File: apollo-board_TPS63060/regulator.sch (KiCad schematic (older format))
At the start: 45 parts, among them J11 Conn_01x04_Male, Q10 2N7002A, Q11 2N7002A, Q13 DMP2035UVT, Q14 DMP2035UVT, Q5 DMP2035UVT, Q9 2N7002A, U10 TPS63070RNMT, U9 TPS63060

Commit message: Place and route U9 (TPS63060)
+ re-place other parts
+ re-design planes shapes
+ display some silkscreen Ref. Des
+ misc. improvements.
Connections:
- net labels added: 3v3_Reg_FB, 3v3_Reg_PS, 3v3_Reg_Vaux, 3v3_Reg_Vin
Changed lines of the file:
@@
 Wire Wire Line
 	7950 1750 8150 1750
-Text Notes 5750 1650 0    50   ~ 0
+Text Notes 5750 1600 0    50   ~ 0
 PS (Power Save Mode) :\n- "0" Enabled\n- "1" Disabled
 Text Notes 7350 2750 0    50   ~ 0
@@
 R1 = R2 x (Vout / Vfb - 1)\nwith Vfb = 500mV
 Wire Notes Line
-	6850 2100 6200 2100
+	6850 2050 6200 2050
 Wire Notes Line
-	6200 2100 6200 1650
+	6200 2050 6200 1650
 Wire Notes Line
 	7600 2300 7600 2500
@@
 Wire Notes Line
 	8250 1550 8250 850
+Text Label 4950 1700 0    50   ~ 0
+3v3_Reg_Vin
+Text Label 6350 1950 0    50   ~ 0
+3v3_Reg_Vaux
+Text Label 8200 2100 0    50   ~ 0
+3v3_Reg_FB
+Text Label 6850 2150 2    50   ~ 0
+3v3_Reg_PS
 $EndSCHEMATC

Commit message: Add TPS63060 component files
+ 3D package
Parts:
- removed U9: TPS63060, Package_SON:Texas_S-PWSON-N10_ThermalVias, symbol Regulator_Switching:TPS63060
- added U9: TPS63060, TPS63060:Texas_S-PWSON-N10_ThermalVias, symbol tps63060:TPS63060
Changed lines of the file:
@@
 Wire Wire Line
 	1850 6800 2450 6800
-$Comp
-L Regulator_Switching:TPS63060 U9
-U 1 1 6035D0EB
-P 7250 1950
-F 0 "U9" H 7250 2617 50  0000 C CNN
-F 1 "TPS63060" H 7250 2526 50  0000 C CNN
-F 2 "Package_SON:Texas_S-PWSON-N10_ThermalVias" H 7250 1300 50  0001 C CNN
-F 3 "http://www.ti.com/lit/ds/symlink/tps63060.pdf" H 7250 1950 50  0001 C CNN
-	1    7250 1950
-	1    0    0    -1
-$EndComp
 Wire Wire Line
 	6850 1550 6750 1550
@@
 Text Label 6850 2150 2    50   ~ 0
 3v3_Reg_PS
+$Comp
+L tps63060:TPS63060 U9
+U 1 1 60371E4B
+P 7250 1950
+F 0 "U9" H 7250 2617 50  0000 C CNN
+F 1 "TPS63060" H 7250 2526 50  0000 C CNN
+F 2 "TPS63060:Texas_S-PWSON-N10_ThermalVias" H 7250 1300 50  0001 C CNN
+F 3 "http://www.ti.com/lit/ds/symlink/tps63060.pdf" H 7250 1950 50  0001 C CNN
+	1    7250 1950
+	1    0    0    -1
+$EndComp
 $EndSCHEMATC

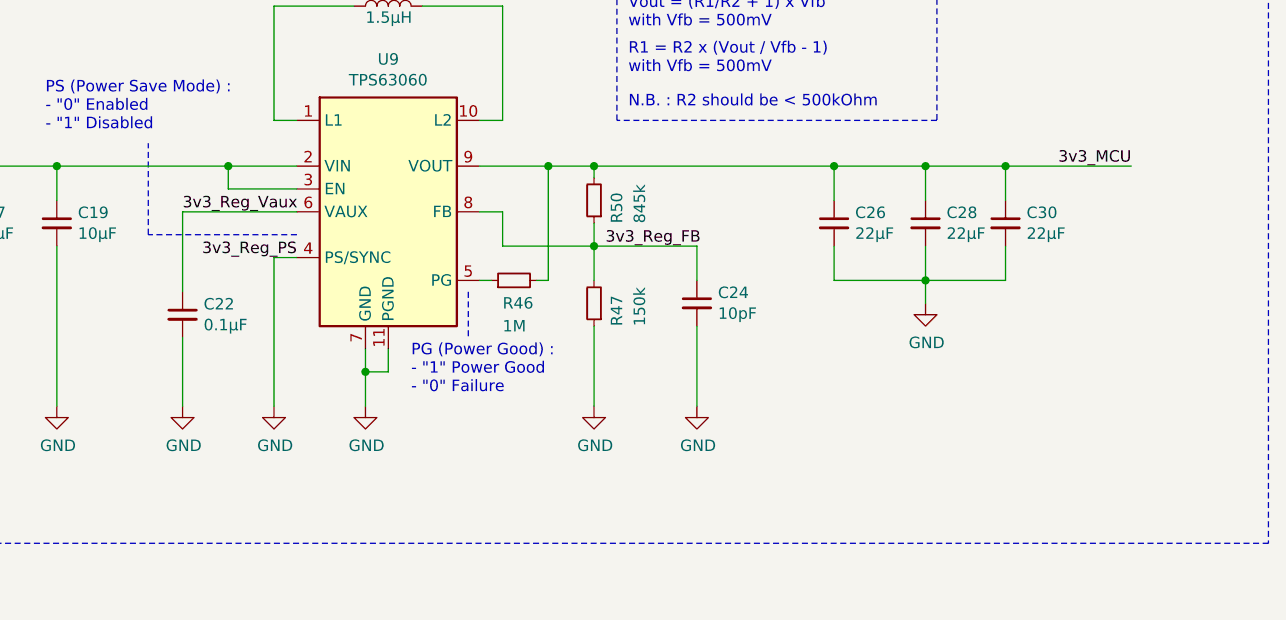
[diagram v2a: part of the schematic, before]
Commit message: Update 22µF 0805 & 100nF 0603 capacitors
around TPS63060
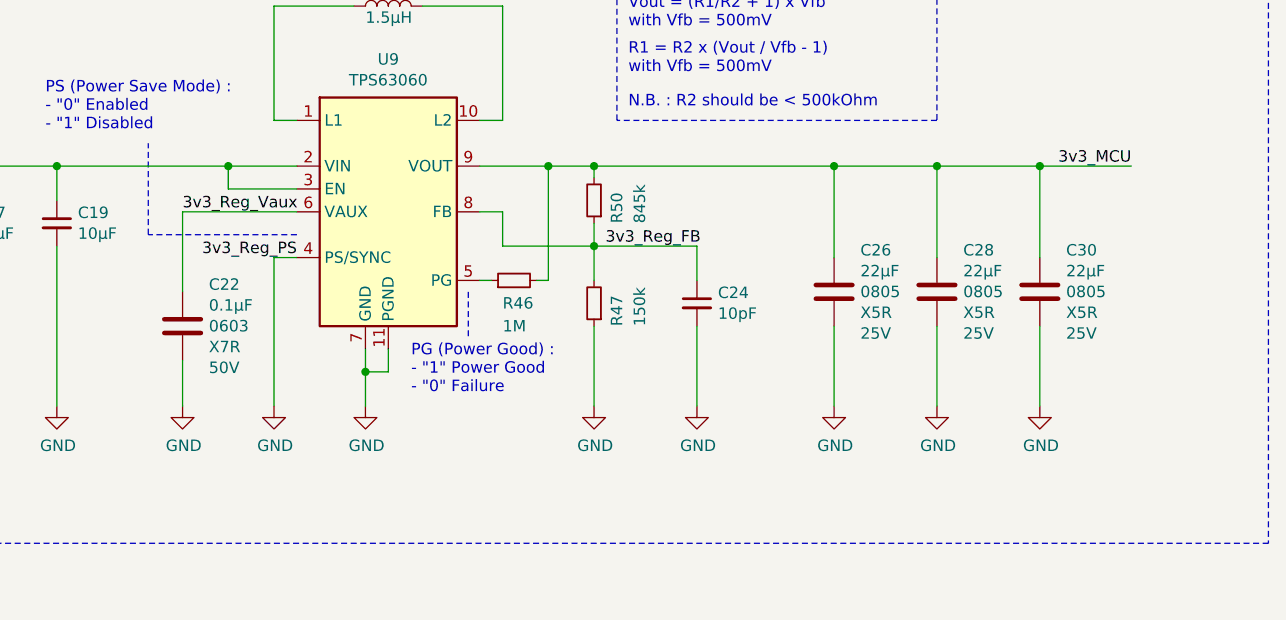
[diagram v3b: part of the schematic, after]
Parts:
- removed C22: 0.1µF, Capacitor_SMD:C_0603_1608Metric, symbol Device:C_Small
- removed C26, C28, C30: 22μF, Capacitor_SMD:C_0805_2012Metric, symbol Device:C_Small
- added C22: CL10B104KB8NNNC, Capacitor_SMD:C_0603_1608Metric, symbol cl10b104kb8nnnc:CL10B104KB8NNNC
- added C26, C28, C30: CL21A226MAQNNNE, Capacitor_SMD:C_0805_2012Metric, symbol cl21a226maqnnne:CL21A226MAQNNNE
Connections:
- net 3v3_MCU: now also C26.1, C28.1, C30.1
- net 3v3_Reg_Vaux: now also C22.1
- net GND: now also C22.2, C26.2, C28.2, C30.2

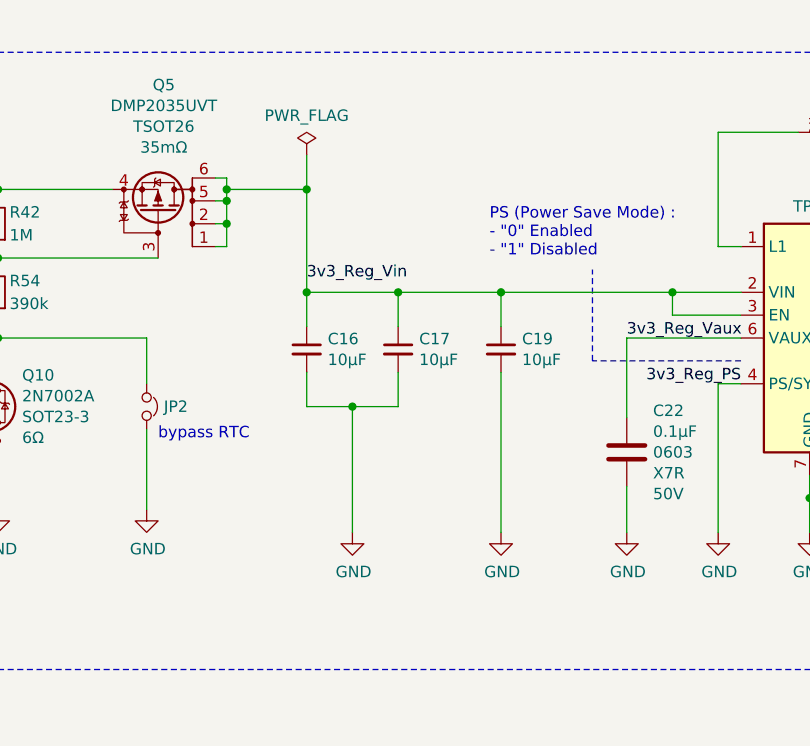
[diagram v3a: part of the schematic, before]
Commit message: Update 10µF 0805 capacitors
Around TPS63060
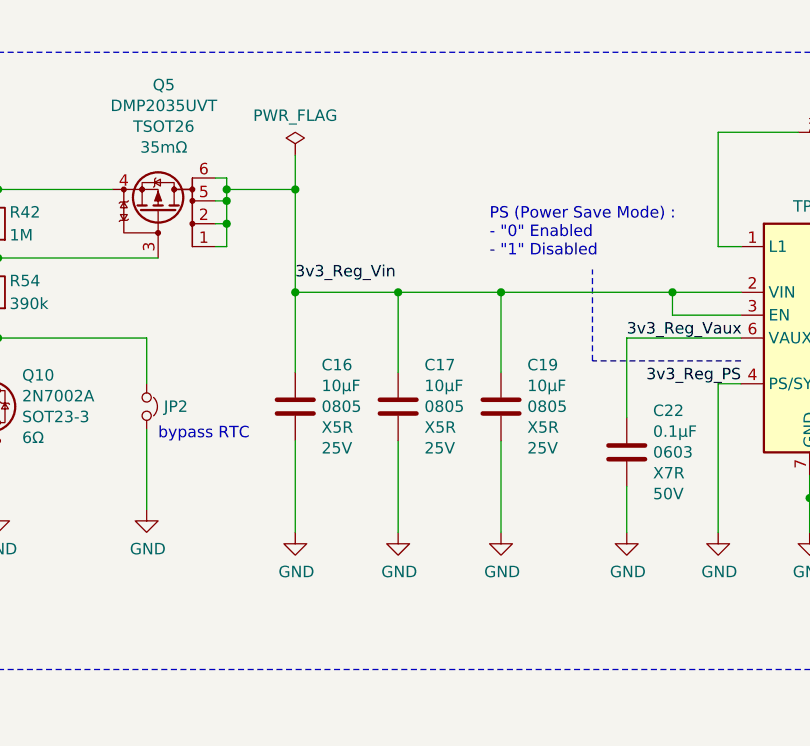
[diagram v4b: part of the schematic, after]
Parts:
- removed C16, C17, C19: 10μF, Capacitor_SMD:C_0805_2012Metric, symbol Device:C_Small
- added C16, C17, C19: CL21A106KAYNNNE, Capacitor_SMD:C_0805_2012Metric, symbol cl21a106kaynnne:CL21A106KAYNNNE
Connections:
- net 3v3_Reg_Vin: now also C16.1, C17.1, C19.1
- net GND: now also C16.2, C17.2, C19.2

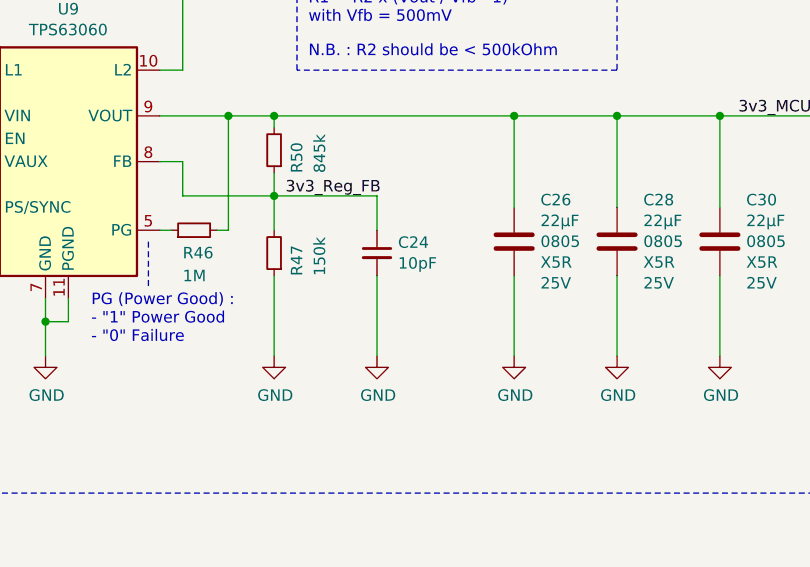
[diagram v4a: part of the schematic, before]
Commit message: Update 10pF 0603 capacitor
around TPS63060
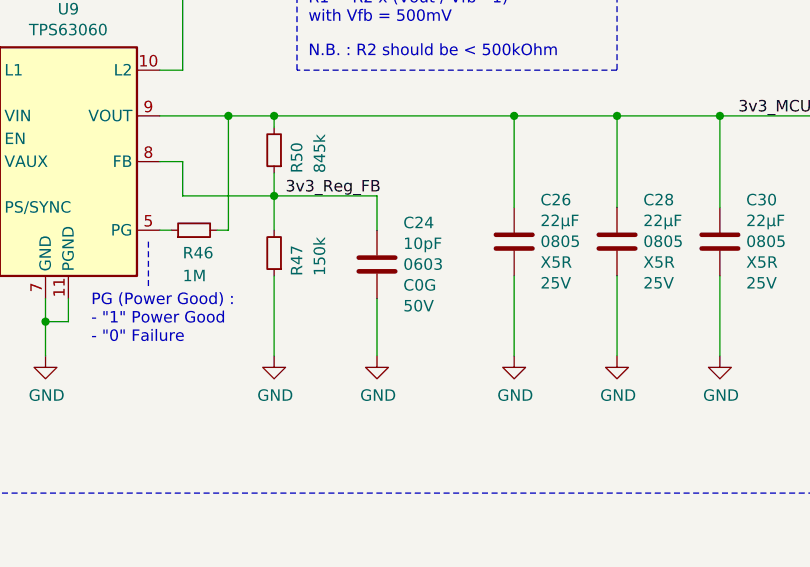
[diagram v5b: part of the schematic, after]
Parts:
- removed C24: 10pF, Capacitor_SMD:C_0603_1608Metric, symbol Device:C_Small
- added C24: CC0603JRNPO9BN100, Capacitor_SMD:C_0603_1608Metric, symbol cc0603jrnpo9bn100:CC0603JRNPO9BN100
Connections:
- net 3v3_Reg_FB: now also C24.1
- net GND: now also C24.2
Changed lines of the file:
@@
-$EndComp
-$Comp
-L Device:C_Small C24
-U 1 1 5FF33363
-P 8600 2350
-F 0 "C24" H 8692 2396 50  0000 L CNN
-F 1 "10pF" H 8692 2305 50  0000 L CNN
-F 2 "Capacitor_SMD:C_0603_1608Metric" H 8600 2350 50  0001 C CNN
-F 3 "~" H 8600 2350 50  0001 C CNN
-	1    8600 2350
-	1    0    0    -1
 $EndComp
 $Comp
@@
 $EndComp
 Wire Wire Line
-	8600 2450 8600 2800
+	8600 2550 8600 2800
 $Comp
 L power:GND #PWR079
@@
 Wire Wire Line
 	4900 2800 4900 2400
+$Comp
+L cc0603jrnpo9bn100:CC0603JRNPO9BN100 C24
+U 1 1 604E718C
+P 8600 2400
+F 0 "C24" H 8715 2582 50  0000 L CNN
+F 1 "CC0603JRNPO9BN100" H 8625 2300 50  0001 L CNN
+F 2 "Capacitor_SMD:C_0603_1608Metric" H 8638 2250 50  0001 C CNN
+F 3 "https://www.mouser.fr/datasheet/2/447/yageo_yago_s_a0009251638_1-1991554.pdf" H 8600 2400 50  0001 C CNN
+F 4 "Yageo" H 8600 2400 50  0001 C CNN "Mfr_name"
+F 5 "CC0603JRNPO9BN100" H 8600 2400 50  0001 C CNN "Mfr_no"
+F 6 "10pF" H 8715 2491 50  0000 L CNN "cap_Value"
+F 7 "0603" H 8715 2400 50  0000 L CNN "Package"
+F 8 "C0G" H 8715 2309 50  0000 L CNN "cap_Dielectric"
+F 9 "50V" H 8715 2218 50  0000 L CNN "cap_Voltage"
+F 10 "https://octopart.com/cc0603jrnpo9bn100-yageo-39467668?r=sp#PriceAndStock" H 8600 2400 50  0001 C CNN "Octopart_link"
+F 11 "https://fr.farnell.com/yageo/cc0603jrnpo9bn100/cond-10pf-50v-5-c0g-np0-0603/dp/721967?st=CC0603JRNPO9BN100" H 8600 2400 50  0001 C CNN "Farnell_link"
+F 12 "721967" H 8600 2400 50  0001 C CNN "Farnell_ref"
+F 13 "2021-02-24" H 8600 2400 50  0001 C CNN "Farnell_check_date"
+F 14 "-" H 8600 2400 50  0001 C CNN "Farnell_price_qt=1"
+F 15 "0,0405 €" H 8600 2400 50  0001 C CNN "Farnell_price_qt=10"
+F 16 "0,0203 €" H 8600 2400 50  0001 C CNN "Farnell_price_qt=100"
+F 17 "0,0135 €" H 8600 2400 50  0001 C CNN "Farnell_price_qt=1000"
+F 18 "1,951,669" H 8600 2400 50  0001 C CNN "Farnell_stock"
+F 19 "https://lcsc.com/product-detail/Multilayer-Ceramic-Capacitors-MLCC-SMD-SMT_YAGEO-CC0603JRNPO9BN100_C106245.html" H 8600 2400 50  0001 C CNN "LCSC_link"
+F 20 "C106245" H 8600 2400 50  0001 C CNN "LCSC_ref"
+F 21 "2021-02-24" H 8600 2400 50  0001 C CNN "LCSC_check_date"
+F 22 "-" H 8600 2400 50  0001 C CNN "LCSC_price_qt=1"
+F 23 "-" H 8600 2400 50  0001 C CNN "LCSC_price_qt=10"
+F 24 "$0.0038" H 8600 2400 50  0001 C CNN "LCSC_price_qt=100"
+F 25 "$0.0029" H 8600 2400 50  0001 C CNN "LCSC_price_qt=1000"
+F 26 "1,595,200" H 8600 2400 50  0001 C CNN "LCSC_stock"
+F 27 "https://www.mouser.fr/ProductDetail/Yageo/CC0603JRNPO9BN100/?qs=%2Fha2pyFaduiZbois2HzNxfUPtExZ87ifpI77BjZxylV95W8Cxrl2Iw%3D%3D" H 8600 2400 50  0001 C CNN "Mouser_link"
+F 28 "603-C0603JRNPO9BN100" H 8600 2400 50  0001 C CNN "Mouser_ref"
+F 29 "2021-02-24" H 8600 2400 50  0001 C CNN "Mouser_check_date"
+F 30 "$0.238" H 8600 2400 50  0001 C CNN "Mouser_price_qt=1"
+F 31 "-" H 8600 2400 50  0001 C CNN "Mouser_price_qt=10"
+F 32 "-" H 8600 2400 50  0001 C CNN "Mouser_price_qt=100"
+F 33 "-" H 8600 2400 50  0001 C CNN "Mouser_price_qt=1000"
+F 34 "494,335" H 8600 2400 50  0001 C CNN "Mouser_stock"
+F 35 "https://fr.rs-online.com/web/p/condensateurs-ceramique-multicouches/2006466/" H 8600 2400 50  0001 C CNN "RS_link"
+F 36 "200-6466" H 8600 2400 50  0001 C CNN "RS_ref"
+F 37 "2021-02-24" H 8600 2400 50  0001 C CNN "RS_check_date"
+F 38 "-" H 8600 2400 50  0001 C CNN "RS_price_qt=1"
+F 39 "-" H 8600 2400 50  0001 C CNN "RS_price_qt=10"
+F 40 "-" H 8600 2400 50  0001 C CNN "RS_price_qt=100"
+F 41 "0,006 € (qt=4000)" H 8600 2400 50  0001 C CNN "RS_price_qt=1000"
+F 42 "-" H 8600 2400 50  0001 C CNN "RS_stock"
+F 43 "TO_CHECK" H 8600 2400 50  0001 C CNN "Status"
+F 44 "1.03" H 8600 2400 50  0001 C CNN "Release_version"
+F 45 "2020-12-21" H 8600 2400 50  0001 C CNN "Release_date"
+F 46 "ManWithNoName" H 8600 2400 50  0001 C CNN "Designer"
+	1    8600 2400
+	1    0    0    -1
+$EndComp
 $EndSCHEMATC

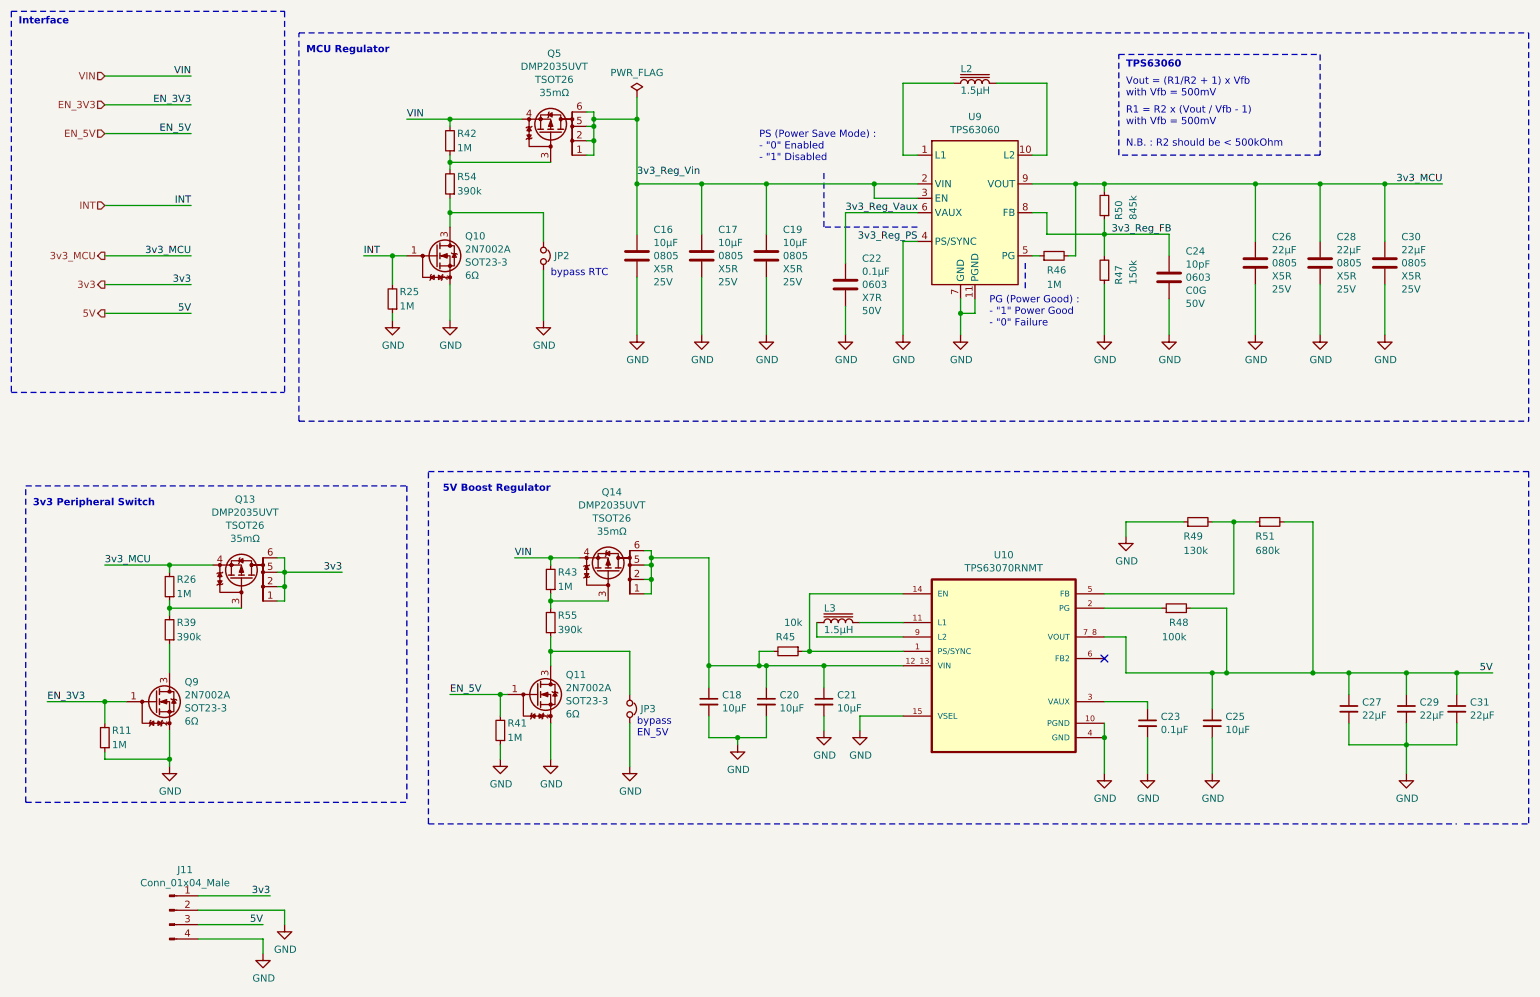
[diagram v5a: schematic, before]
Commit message: Place and route the 2nd TPS63060 (+5V)
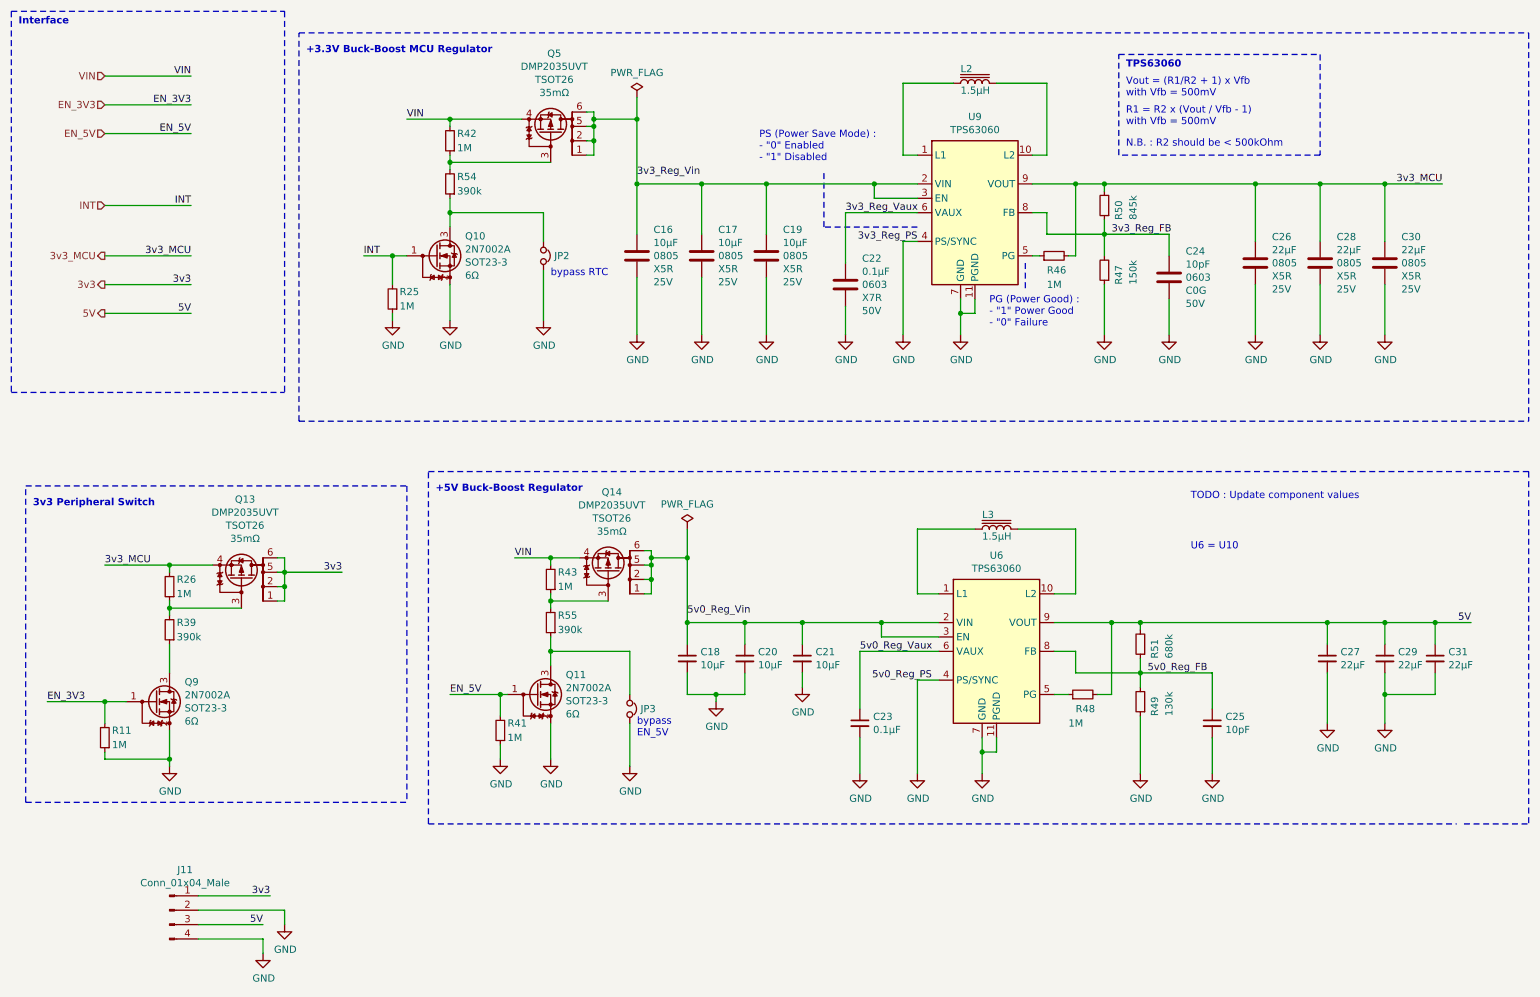
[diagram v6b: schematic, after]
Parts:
- removed R45: 10k, Resistor_SMD:R_0603_1608Metric, symbol Device:R_Small
- removed U10: TPS63070RNMT, TPS63070RNM:VREG_TPS63070RNMR, symbol TPS63070NRM:TPS63070RNMT
- added U6: TPS63060, TPS63060:Texas_S-PWSON-N10_ThermalVias, symbol tps63060:TPS63060
- C25: value 10μF -> 10pF; footprint Capacitor_SMD:C_0805_2012Metric -> Capacitor_SMD:C_0603_1608Metric
- R48: value 100k -> 1M
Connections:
- net 5V: now also U6.9 (VOUT); no longer C25.1
- net GND: now also U6.11 (PGND), U6.4 (PS/SYNC), U6.7 (GND)
- net at L3.1: now also U6.1 (L1)
- net at L3.2: now also U6.10 (L2)
- net 5v0_Reg_Vin: now reaches C18.1, C20.1, C21.1, Q14.1 (D), Q14.2 (D), Q14.5 (D), Q14.6 (D)
- net 5v0_Reg_Vin: now also U6.2 (VIN), U6.3 (EN)
- net at R48.1: now also U6.5 (PG)
- net 5v0_Reg_FB: now reaches R49.2, R51.1
- net 5v0_Reg_FB: now also C25.1, U6.8 (FB)
- net 5v0_Reg_Vaux: now reaches C23.1
- net 5v0_Reg_Vaux: now also U6.6 (VAUX)
- no-connect marks 1 -> 0
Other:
- note added: "+3.3V Buck-Boost MCU Regulator"
- note added: "+5V Buck-Boost Regulator"
- note added: "TODO : Update component values"
- note added: "U6 = U10"
- note removed: "5V Boost Regulator"
- note removed: "MCU Regulator"
- moved on the sheet: C18, C20, C21, C23, C27, C29, C31, L3, R48, R49, R51
